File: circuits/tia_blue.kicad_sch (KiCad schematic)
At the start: 11 parts, among them U4 OPA380AID

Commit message: Checkpoint laser controller fab parity package
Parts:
- removed R14: 1k, Resistor_SMD:R_0603_1608Metric_Pad0.98x0.95mm_HandSolder, symbol viv:R_H
- added RV8: RF 2M, Potentiometer_SMD:Potentiometer_Bourns_3224W_Vertical, symbol viv:POT_H
- R14: renamed from RV8; value RF 2M -> 1k; footprint Potentiometer_SMD:Potentiometer_Bourns_3224W_Vertical -> Resistor_SMD:R_0603_1608Metric_Pad0.98x0.95mm_HandSolder; symbol viv:POT_H -> viv:R_H; LCSC C116323 -> C2907002; Part Number 3224W-1-205E -> FRC0603F1001TS
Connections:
- net +5V: now also R14.1
- net V_OUT: now also RV8.2 (W), RV8.3; no longer R14.2 (W), R14.3
- net PD_CATHODE: now reaches C15.1, D4.1 (K)
- net PD_CATHODE: now also R14.2
- net PD_ANODE: now reaches C13.1, D4.2 (A), U4.2 (-)
- net PD_ANODE: now also RV8.1; no longer R14.1
- net VBIAS: now reaches C16.1, R15.2, U4.3 (+)
- net VBIAS_TOP: now reaches R16.2, RV4.1
- net VBIAS_WIPER: now reaches R15.1, RV4.2 (W)
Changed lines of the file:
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@@
   (no_connect (at 224.79 154.94))
   (no_connect (at 224.79 144.78))
+  (label "PD_ANODE" (at 190.5 130.81 0) (effects (font (size 1.27 1.27)) (justify left bottom)))
+  (label "PD_CATHODE" (at 185.42 130.81 0) (effects (font (size 1.27 1.27)) (justify left bottom)))
+  (label "VBIAS_TOP" (at 165.1 143.51 0) (effects (font (size 1.27 1.27)) (justify left bottom)))
+  (label "VBIAS_WIPER" (at 168.91 152.4 0) (effects (font (size 1.27 1.27)) (justify left bottom)))
+  (label "VBIAS" (at 190.5 152.4 0) (effects (font (size 1.27 1.27)) (justify left bottom)))
   (hierarchical_label "V_OUT" (shape output) (at 232.41 149.86 0) (effects (font (size 1.27 1.27)) (justify left)))
   (text "TIA Channel  —  on-board SFH2201 signal PD → OPA380AID transimpedance amp  ·  reused 4× (IR / RED / GREEN / BLUE)" (at 150 104 0) (effects (font (size 2.0 2.0)) (justify left)))

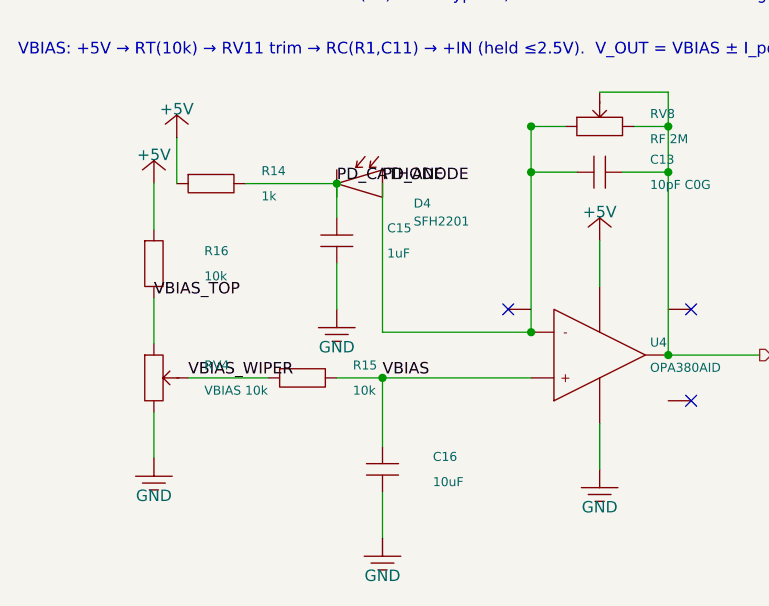
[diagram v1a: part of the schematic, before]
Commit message: Checkpoint schematic warning hygiene
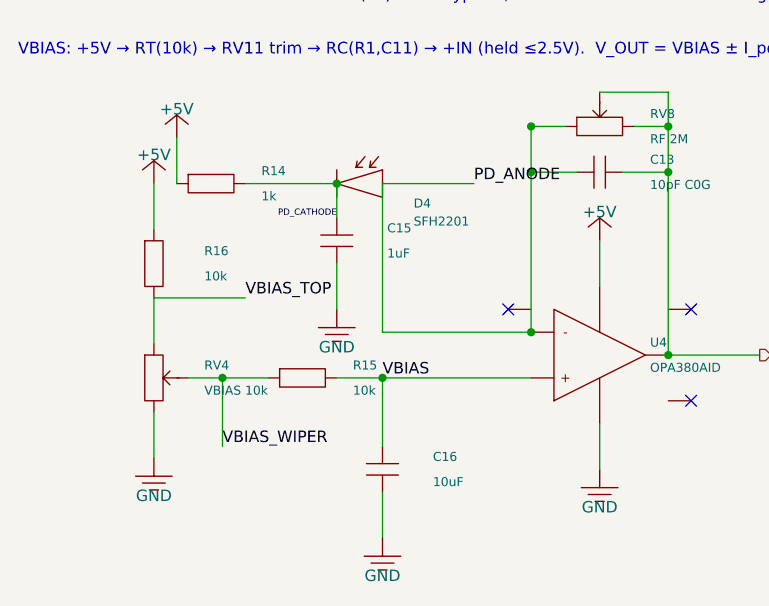
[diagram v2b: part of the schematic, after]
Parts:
- removed R14: 1k, Resistor_SMD:R_0603_1608Metric_Pad0.98x0.95mm_HandSolder, symbol viv:R_H
- added RV8: RF 2M, Potentiometer_SMD:Potentiometer_Bourns_3224W_Vertical, symbol viv:POT_H
- R14: renamed from RV8; value RF 2M -> 1k; footprint Potentiometer_SMD:Potentiometer_Bourns_3224W_Vertical -> Resistor_SMD:R_0603_1608Metric_Pad0.98x0.95mm_HandSolder; symbol viv:POT_H -> viv:R_H; LCSC C116323 -> C2907002; Part Number 3224W-1-205E -> FRC0603F1001TS
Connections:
- net +5V: now also R14.1
- net PD_ANODE: now also RV8.1; no longer R14.1
- net PD_CATHODE: now also R14.2
- net V_OUT: now also RV8.2 (W), RV8.3; no longer R14.2 (W), R14.3
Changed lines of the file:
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@@
   (wire (pts (xy 167.64 130.81) (xy 167.64 125.73)) (stroke (width 0) (type default)))
   (wire (pts (xy 185.42 139.7) (xy 185.42 144.78)) (stroke (width 0) (type default)))
+  (wire (pts (xy 190.5 130.81) (xy 200.66 130.81)) (stroke (width 0) (type default)))
   (wire (pts (xy 207.01 147.32) (xy 207.01 129.54)) (stroke (width 0) (type default)))
   (wire (pts (xy 207.01 129.54) (xy 207.01 124.46)) (stroke (width 0) (type default)))
@@
   (wire (pts (xy 190.5 165.1) (xy 190.5 170.18)) (stroke (width 0) (type default)))
   (wire (pts (xy 165.1 143.51) (xy 165.1 148.59)) (stroke (width 0) (type default)))
-  (wire (pts (xy 168.91 152.4) (xy 177.8 152.4)) (stroke (width 0) (type default)))
+  (wire (pts (xy 168.91 152.4) (xy 172.72 152.4)) (stroke (width 0) (type default)))
+  (wire (pts (xy 172.72 152.4) (xy 177.8 152.4)) (stroke (width 0) (type default)))
   (wire (pts (xy 185.42 152.4) (xy 190.5 152.4)) (stroke (width 0) (type default)))
   (wire (pts (xy 190.5 152.4) (xy 190.5 160.02)) (stroke (width 0) (type default)))
   (wire (pts (xy 190.5 152.4) (xy 207.01 152.4)) (stroke (width 0) (type default)))
+  (wire (pts (xy 165.1 143.51) (xy 175.26 143.51)) (stroke (width 0) (type default)))
+  (wire (pts (xy 172.72 152.4) (xy 172.72 160.02)) (stroke (width 0) (type default)))
   (junction (at 207.01 147.32) (diameter 0) (color 0 0 0 0))
   (junction (at 185.42 130.81) (diameter 0) (color 0 0 0 0))
@@
   (junction (at 222.25 149.86) (diameter 0) (color 0 0 0 0))
   (junction (at 190.5 152.4) (diameter 0) (color 0 0 0 0))
+  (junction (at 172.72 152.4) (diameter 0) (color 0 0 0 0))
   (no_connect (at 204.47 144.78))
   (no_connect (at 224.79 154.94))
   (no_connect (at 224.79 144.78))
-  (label "PD_ANODE" (at 190.5 130.81 0) (effects (font (size 1.27 1.27)) (justify left bottom)))
-  (label "PD_CATHODE" (at 185.42 130.81 0) (effects (font (size 1.27 1.27)) (justify left bottom)))
-  (label "VBIAS_TOP" (at 165.1 143.51 0) (effects (font (size 1.27 1.27)) (justify left bottom)))
-  (label "VBIAS_WIPER" (at 168.91 152.4 0) (effects (font (size 1.27 1.27)) (justify left bottom)))
+  (label "PD_ANODE" (at 200.66 130.81 0) (effects (font (size 1.27 1.27)) (justify left bottom)))
+  (label "PD_CATHODE" (at 185.42 134.62 0) (effects (font (size 0.7 0.7)) (justify right bottom)))
+  (label "VBIAS_TOP" (at 175.26 143.51 0) (effects (font (size 1.27 1.27)) (justify left bottom)))
+  (label "VBIAS_WIPER" (at 172.72 160.02 0) (effects (font (size 1.27 1.27)) (justify left bottom)))
   (label "VBIAS" (at 190.5 152.4 0) (effects (font (size 1.27 1.27)) (justify left bottom)))
   (hierarchical_label "V_OUT" (shape output) (at 232.41 149.86 0) (effects (font (size 1.27 1.27)) (justify left)))
